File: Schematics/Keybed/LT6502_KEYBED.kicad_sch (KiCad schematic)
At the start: 25 parts, among them J14 KeyConn, J4 Conn_02x05_Odd_Even, Q3 STL9P3LLH6, U1 ATmega644P-20P, U2 74HC138, X2 CXO_DIP8

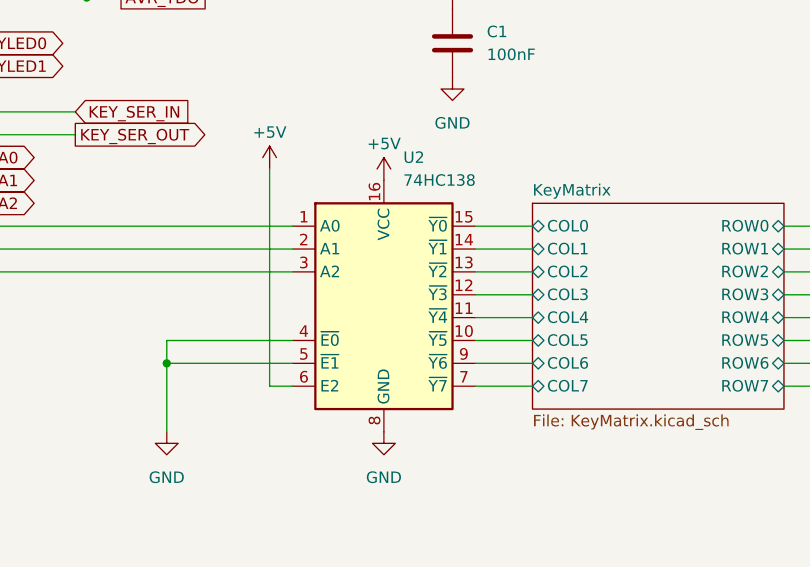
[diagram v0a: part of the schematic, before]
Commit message: Routing Completed
Routing completed, removed silkscreen IDs for clarity
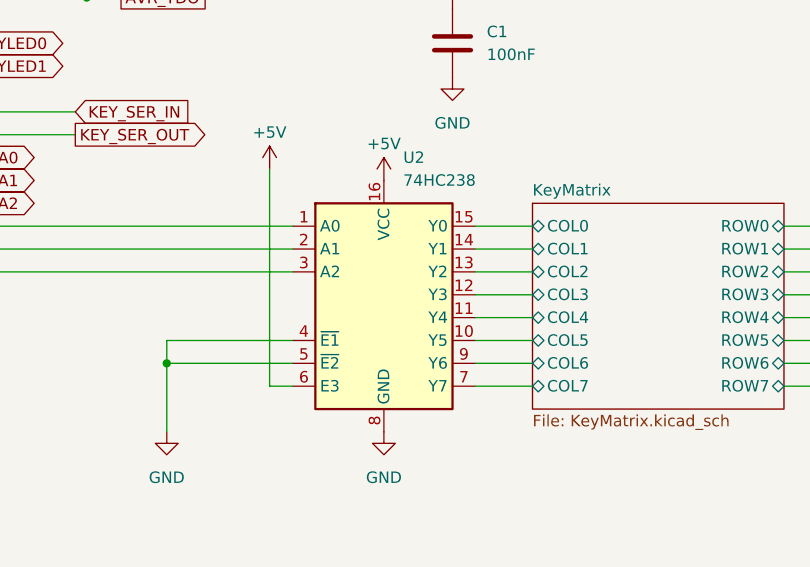
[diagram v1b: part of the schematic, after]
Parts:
- removed U2: 74HC138, Package_SO:SSOP-16_5.3x6.2mm_P0.65mm, symbol 74xx:74HC138
- added U2: 74HC238, Package_SO:SSOP-16_5.3x6.2mm_P0.65mm, symbol 74xx:74HC238
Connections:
- net +5V: now also U2.16 (VCC), U2.6 (E3)
- net GND: now also U2.4 (~{E1}), U2.5 (~{E2}), U2.8 (GND)
- net KeyMatrix/COL0: now also U2.15 (Y0)
- net KeyMatrix/COL1: now also U2.14 (Y1)
- net KeyMatrix/COL2: now also U2.13 (Y2)
- net KeyMatrix/COL3: now also U2.12 (Y3)
- net KeyMatrix/COL4: now also U2.11 (Y4)
- net KeyMatrix/COL5: now also U2.10 (Y5)
- net KeyMatrix/COL6: now also U2.9 (Y6)
- net KeyMatrix/COL7: now also U2.7 (Y7)
- net at U1.19 (PD5): now also U2.1 (A0)
- net at U1.20 (PD6): now also U2.2 (A1)
- net at U1.21 (PD7): now also U2.3 (A2)
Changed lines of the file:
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@@
 	)
 	(symbol
+		(lib_id "74xx:74HC238")
+		(at 128.27 128.27 0)
+		(unit 1)
+		(exclude_from_sim no)
+		(in_bom yes)
+		(on_board yes)
+		(dnp no)
+		(fields_autoplaced yes)
+		(property "Reference" "U2"
+			(at 130.4133 110.49 0)
+			(effects
+				(font
+					(size 1.27 1.27)
+				)
+				(justify left)
+			)
+		)
+		(property "Value" "74HC238"
+			(at 130.4133 113.03 0)
+			(effects
+				(font
+					(size 1.27 1.27)
+				)
+				(justify left)
+			)
+		)
+		(property "Footprint" "Package_SO:SSOP-16_5.3x6.2mm_P0.65mm"
+			(at 128.27 128.27 0)
+			(effects
+				(font
+					(size 1.27 1.27)
+				)
+				(hide yes)
+			)
+		)
+		(property "Datasheet" "https://www.ti.com/lit/ds/symlink/cd74hc238.pdf"
+			(at 128.27 128.27 0)
+			(effects
+				(font
+					(size 1.27 1.27)
+				)
+				(hide yes)
+			)
+		)
+		(property "Description" "3-to-8 line decoder/multiplexer, DIP-16/SOIC-16/SSOP-16"
+			(at 128.27 128.27 0)
+			(effects
+				(font
+					(size 1.27 1.27)
+				)
+				(hide yes)
+			)
+		)
+		(pin "14"
+		)
+		(pin "13"
+		)
+		(pin "8"
+		)
+		(pin "9"
+		)
+		(pin "1"
+		)
+		(pin "2"
+		)
+		(pin "3"
+		)
+		(pin "6"
+		)
+		(pin "12"
+		)
+		(pin "15"
+		)
+		(pin "16"
+		)
+		(pin "7"
+		)
+		(pin "10"
+		)
+		(pin "11"
+		)
+		(pin "4"
+		)
+		(pin "5"
+		)
+		(instances
+			(project ""
+				(path "/df3f2d3f-c20b-413e-9d55-4328b6be904e"
+					(reference "U2")
+					(unit 1)
+				)
+			)
+		)
+	)
+	(symbol
 		(lib_id "power:+5V")
 		(at 17.78 50.8 0)
@@
 					(unit 1)
 				)
-			)
-		)
-	)
-	(symbol
-		(lib_id "74xx:74HC138")
-		(at 128.27 128.27 0)
-		(unit 1)
-		(exclude_from_sim no)
-		(in_bom yes)
-		(on_board yes)
-		(dnp no)
-		(fields_autoplaced yes)
-		(property "Reference" "U2"
-			(at 130.4133 110.49 0)
-			(effects
-				(font
-					(size 1.27 1.27)
-				)
-				(justify left)
-			)
-		)
-		(property "Value" "74HC138"
-			(at 130.4133 113.03 0)
-			(effects
-				(font
-					(size 1.27 1.27)
-				)
-				(justify left)
-			)
-		)
-		(property "Footprint" "Package_SO:SSOP-16_5.3x6.2mm_P0.65mm"
-			(at 128.27 128.27 0)
-			(effects
-				(font
-					(size 1.27 1.27)
-				)
-				(hide yes)
-			)
-		)
-		(property "Datasheet" "http://www.ti.com/lit/ds/symlink/cd74hc238.pdf"
-			(at 128.27 128.27 0)
-			(effects
-				(font
-					(size 1.27 1.27)
-				)
-				(hide yes)
-			)
-		)
-		(property "Description" "3-to-8 line decoder/multiplexer inverting, DIP-16/SOIC-16/SSOP-16"
-			(at 128.27 128.27 0)
-			(effects
-				(font
-					(size 1.27 1.27)
-				)
-				(hide yes)
-			)
-		)
-		(pin "13"
-		)
-		(pin "12"
-		)
-		(pin "10"
-		)
-		(pin "7"
-		)
-		(pin "16"
-		)
-		(pin "9"
-		)
-		(pin "5"
-		)
-		(pin "6"
-		)
-		(pin "4"
-		)
-		(pin "15"
-		)
-		(pin "14"
-		)
-		(pin "8"
-		)
-		(pin "2"
-		)
-		(pin "11"
-		)
-		(pin "1"
-		)
-		(pin "3"
-		)
-		(instances
-			(project ""
-				(path "/df3f2d3f-c20b-413e-9d55-4328b6be904e"
-					(reference "U2")
-					(unit 1)
-				)

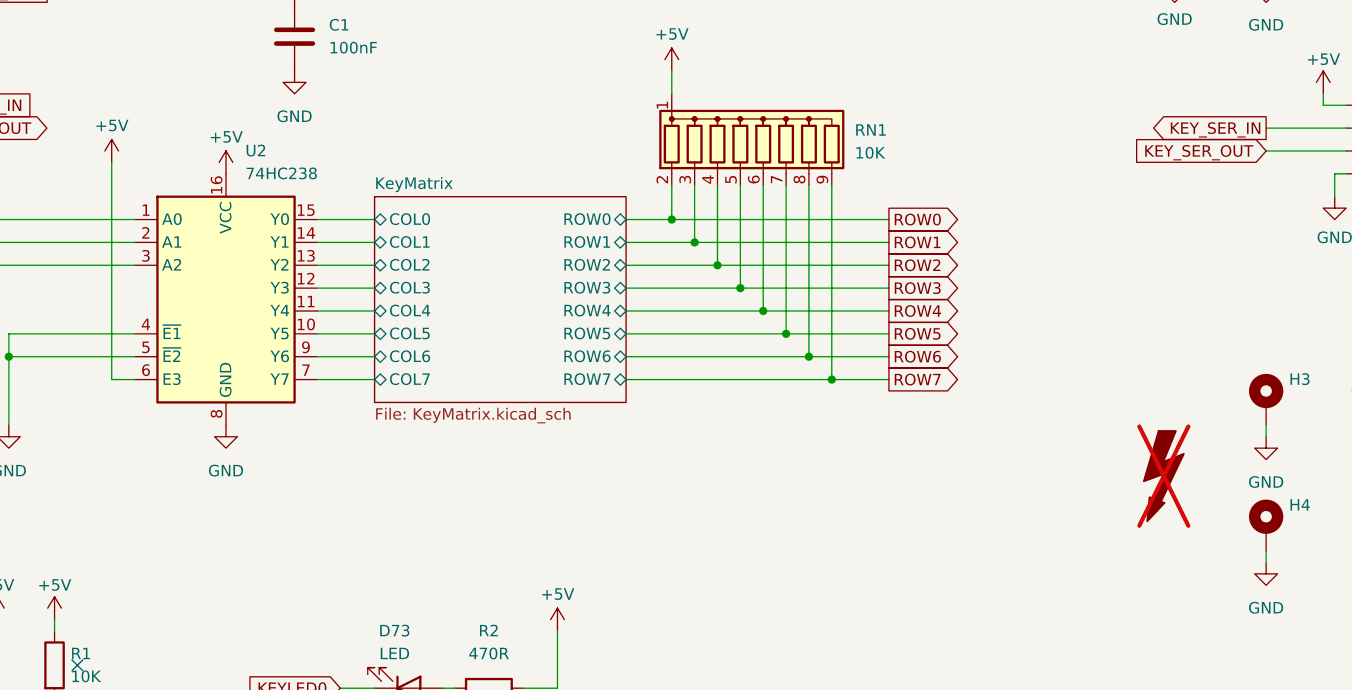
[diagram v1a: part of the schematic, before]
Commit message: Updated BoMs ordered PCBs
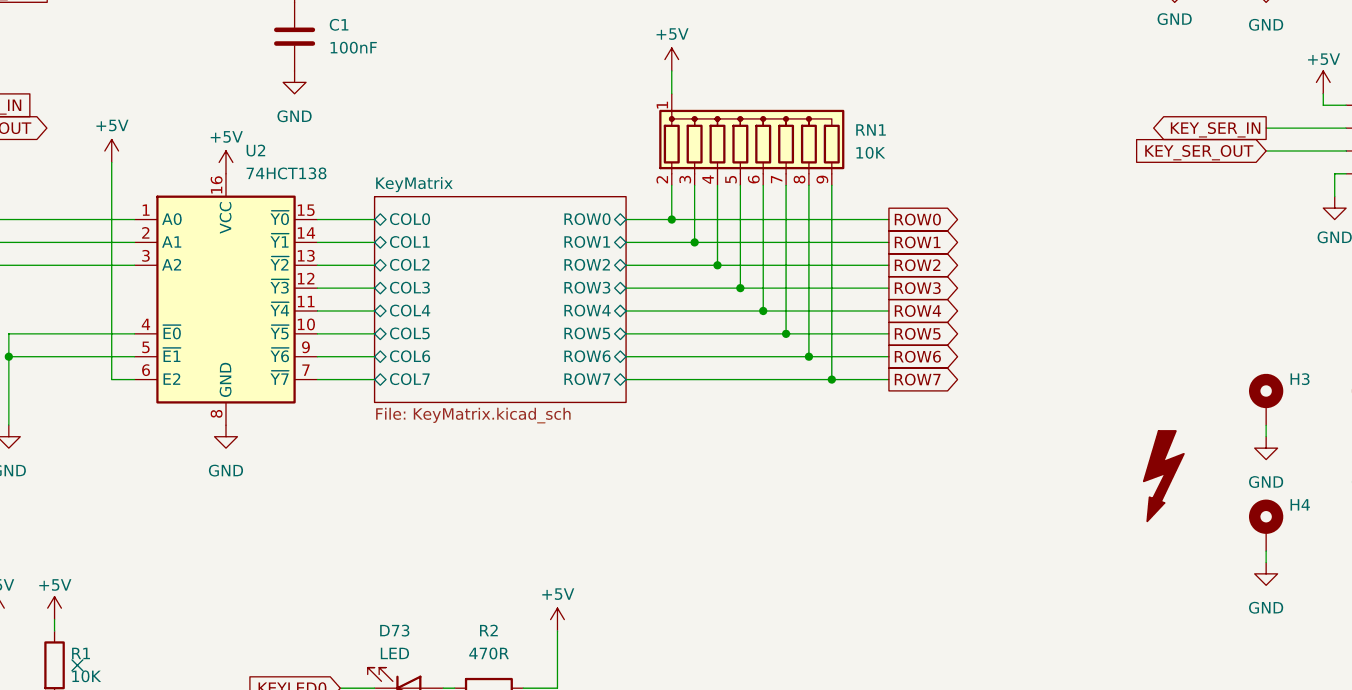
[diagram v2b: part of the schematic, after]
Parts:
- removed U2: 74HC238, Package_SO:SSOP-16_5.3x6.2mm_P0.65mm, symbol 74xx:74HC238
- added U2: 74HCT138, Package_SO:SSOP-16_5.3x6.2mm_P0.65mm, symbol 74xx:74HCT138
- FOX1: now fitted
- J14: LCSC (none) -> DNF
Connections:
- net +5V: now also U2.16 (VCC), U2.6 (E2)
- net GND: now also U2.4 (~{E0}), U2.5 (~{E1}), U2.8 (GND)
- net KeyMatrix/COL0: now also U2.15 (~{Y0})
- net KeyMatrix/COL1: now also U2.14 (~{Y1})
- net KeyMatrix/COL2: now also U2.13 (~{Y2})
- net KeyMatrix/COL3: now also U2.12 (~{Y3})
- net KeyMatrix/COL4: now also U2.11 (~{Y4})
- net KeyMatrix/COL5: now also U2.10 (~{Y5})
- net KeyMatrix/COL6: now also U2.9 (~{Y6})
- net KeyMatrix/COL7: now also U2.7 (~{Y7})
- net at U1.19 (PD5): now also U2.1 (A0)
- net at U1.20 (PD6): now also U2.2 (A1)
- net at U1.21 (PD7): now also U2.3 (A2)
